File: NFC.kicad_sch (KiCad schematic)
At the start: 3 parts, among them U9 ST25DV04KC

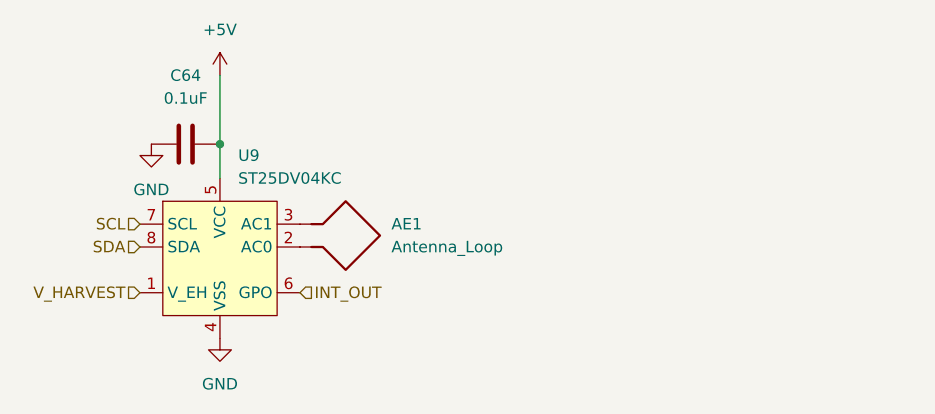
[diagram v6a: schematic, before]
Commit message: added nfc antenna components, added most of footprints
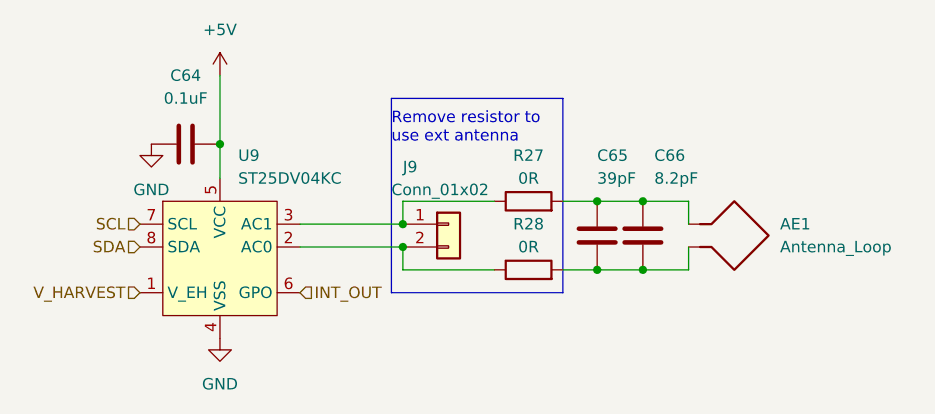
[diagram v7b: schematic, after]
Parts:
- added C65: 39pF, Capacitor_SMD:C_0603_1608Metric_Pad1.08x0.95mm_HandSolder, symbol Device:C
- added C66: 8.2pF, Capacitor_SMD:C_0603_1608Metric_Pad1.08x0.95mm_HandSolder, symbol Device:C
- added J9: Conn_01x02, Connector_PinSocket_2.54mm:PinSocket_1x02_P2.54mm_Vertical, symbol Connector_Generic:Conn_01x02
- added R27, R28: 0R, symbol Device:R
- AE1: footprint (none) -> airsoft_controller:Antenna_loop-13.56MHz
- C64: footprint (none) -> Capacitor_SMD:C_0603_1608Metric_Pad1.08x0.95mm_HandSolder
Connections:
- net at AE1.1: now also C65.1, C66.1, R27.2; no longer U9.3 (AC1)
- net at AE1.2: now also C65.2, C66.2, R28.2; no longer U9.2 (AC0)
- new net: J9.2 (Pin_2), R28.1, U9.2 (AC0)
- new net: J9.1 (Pin_1), R27.1, U9.3 (AC1)
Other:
- note added: "Remove resistor to use ext antenna"
- moved on the sheet: AE1
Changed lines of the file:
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@@
 (kicad_sch (version 20211123) (generator eeschema)
   (paper "A4")
+  (junction (at 187.96 83.82) (diameter 0) (color 0 0 0 0)
+  )
+  (junction (at 187.96 76.2) (diameter 0) (color 0 0 0 0)
+  )
   (junction (at 140.97 69.85) (diameter 0) (color 0 0 0 0)
   )
+  (junction (at 182.88 76.2) (diameter 0) (color 0 0 0 0)
+  )
+  (junction (at 182.88 83.82) (diameter 0) (color 0 0 0 0)
+  )
+  (junction (at 161.29 81.28) (diameter 0) (color 0 0 0 0)
+  )
+  (junction (at 161.29 78.74) (diameter 0) (color 0 0 0 0)
+  )
+  (wire (pts (xy 149.86 81.28) (xy 161.29 81.28))
+    (stroke (width 0) (type default) (color 0 0 0 0))
+  )
+  (wire (pts (xy 171.45 83.82) (xy 161.29 83.82))
+    (stroke (width 0) (type default) (color 0 0 0 0))
+  )
+  (wire (pts (xy 149.86 78.74) (xy 161.29 78.74))
+    (stroke (width 0) (type default) (color 0 0 0 0))
+  )
+  (wire (pts (xy 187.96 76.2) (xy 193.04 76.2))
+    (stroke (width 0) (type default) (color 0 0 0 0))
+  )
+  (polyline (pts (xy 179.07 64.77) (xy 179.07 86.36))
+    (stroke (width 0) (type default) (color 0 0 0 0))
+  )
+  (wire (pts (xy 179.07 76.2) (xy 182.88 76.2))
+    (stroke (width 0) (type default) (color 0 0 0 0))
+  )
+  (wire (pts (xy 161.29 83.82) (xy 161.29 81.28))
+    (stroke (width 0) (type default) (color 0 0 0 0))
+  )
   (wire (pts (xy 140.97 69.85) (xy 140.97 73.66))
     (stroke (width 0) (type default) (color 0 0 0 0))
   )
+  (wire (pts (xy 182.88 83.82) (xy 179.07 83.82))
+    (stroke (width 0) (type default) (color 0 0 0 0))
+  )
+  (wire (pts (xy 193.04 81.28) (xy 193.04 83.82))
+    (stroke (width 0) (type default) (color 0 0 0 0))
+  )
+  (wire (pts (xy 182.88 76.2) (xy 187.96 76.2))
+    (stroke (width 0) (type default) (color 0 0 0 0))
+  )
+  (wire (pts (xy 187.96 83.82) (xy 182.88 83.82))
+    (stroke (width 0) (type default) (color 0 0 0 0))
+  )
+  (polyline (pts (xy 160.02 64.77) (xy 179.07 64.77))
+    (stroke (width 0) (type default) (color 0 0 0 0))
+  )
+  (wire (pts (xy 171.45 76.2) (xy 161.29 76.2))
+    (stroke (width 0) (type default) (color 0 0 0 0))
+  )
+  (wire (pts (xy 193.04 78.74) (xy 193.04 76.2))
+    (stroke (width 0) (type default) (color 0 0 0 0))
+  )
+  (polyline (pts (xy 179.07 86.36) (xy 160.02 86.36))
+    (stroke (width 0) (type default) (color 0 0 0 0))
+  )
+  (polyline (pts (xy 160.02 86.36) (xy 160.02 64.77))
+    (stroke (width 0) (type default) (color 0 0 0 0))
+  )
   (wire (pts (xy 140.97 62.23) (xy 140.97 69.85))
     (stroke (width 0) (type default) (color 0 0 0 0))
+  )
+  (wire (pts (xy 193.04 83.82) (xy 187.96 83.82))
+    (stroke (width 0) (type default) (color 0 0 0 0))
+  )
+  (wire (pts (xy 161.29 76.2) (xy 161.29 78.74))
+    (stroke (width 0) (type default) (color 0 0 0 0))
+  )
+  (text "Remove resistor to\nuse ext antenna" (at 160.02 69.85 0)
+    (effects (font (size 1.27 1.27)) (justify left bottom))
   )
   (hierarchical_label "INT_OUT" (shape input) (at 149.86 86.36 0)
@@
     (pin "1")
   )
-  (symbol (lib_id "Device:Antenna_Loop") (at 154.94 78.74 270) (unit 1)
-    (in_bom yes) (on_board yes) (fields_autoplaced)
-    (property "Reference" "AE1" (id 0) (at 160.02 78.7399 90)
-      (effects (font (size 1.27 1.27)) (justify left))
-    )
-    (property "Value" "Antenna_Loop" (id 1) (at 160.02 81.2799 90)
-      (effects (font (size 1.27 1.27)) (justify left))
-    )
-    (property "Footprint" "" (id 2) (at 154.94 78.74 0)
-      (effects (font (size 1.27 1.27)) hide)
-    )
-    (property "Datasheet" "~" (id 3) (at 154.94 78.74 0)
+  (symbol (lib_id "Device:Antenna_Loop") (at 198.12 78.74 270) (unit 1)
+    (in_bom yes) (on_board yes) (fields_autoplaced)
+    (property "Reference" "AE1" (id 0) (at 203.2 78.7399 90)
+      (effects (font (size 1.27 1.27)) (justify left))
+    )
+    (property "Value" "Antenna_Loop" (id 1) (at 203.2 81.2799 90)
+      (effects (font (size 1.27 1.27)) (justify left))
+    )
+    (property "Footprint" "airsoft_controller:Antenna_loop-13.56MHz" (id 2) (at 198.12 78.74 0)
+      (effects (font (size 1.27 1.27)) hide)
+    )
+    (property "Datasheet" "~" (id 3) (at 198.12 78.74 0)
+      (effects (font (size 1.27 1.27)) hide)
+    )
+    (pin "1")
+    (pin "2")
+  )
+  (symbol (lib_id "Device:C") (at 182.88 80.01 0) (unit 1)
+    (in_bom yes) (on_board yes)
+    (property "Reference" "C65" (id 0) (at 182.88 71.12 0)
+      (effects (font (size 1.27 1.27)) (justify left))
+    )
+    (property "Value" "39pF" (id 1) (at 182.88 73.66 0)
+      (effects (font (size 1.27 1.27)) (justify left))
+    )
+    (property "Footprint" "Capacitor_SMD:C_0603_1608Metric_Pad1.08x0.95mm_HandSolder" (id 2) (at 183.8452 83.82 0)
+      (effects (font (size 1.27 1.27)) hide)
+    )
+    (property "Datasheet" "~" (id 3) (at 182.88 80.01 0)
       (effects (font (size 1.27 1.27)) hide)
     )
@@
     (property "Reference" "C64" (id 0) (at 137.16 62.23 90))
     (property "Value" "0.1uF" (id 1) (at 137.16 64.77 90))
-    (property "Footprint" "" (id 2) (at 140.97 68.8848 0)
+    (property "Footprint" "Capacitor_SMD:C_0603_1608Metric_Pad1.08x0.95mm_HandSolder" (id 2) (at 140.97 68.8848 0)
       (effects (font (size 1.27 1.27)) hide)
     )
@@
       (effects (font (size 1.27 1.27)) hide)
     )
+    (pin "1")
+    (pin "2")
+  )
+  (symbol (lib_id "Connector_Generic:Conn_01x02") (at 166.37 78.74 0) (unit 1)
+    (in_bom yes) (on_board yes)
+    (property "Reference" "J9" (id 0) (at 161.29 72.39 0)
+      (effects (font (size 1.27 1.27)) (justify left))
+    )
+    (property "Value" "Conn_01x02" (id 1) (at 160.02 74.93 0)
+      (effects (font (size 1.27 1.27)) (justify left))
+    )
+    (property "Footprint" "Connector_PinSocket_2.54mm:PinSocket_1x02_P2.54mm_Vertical" (id 2) (at 166.37 78.74 0)
+      (effects (font (size 1.27 1.27)) hide)
+    )
+    (property "Datasheet" "~" (id 3) (at 166.37 78.74 0)
+      (effects (font (size 1.27 1.27)) hide)
+    )
+    (pin "1")
+    (pin "2")
+  )
+  (symbol (lib_id "Device:R") (at 175.26 83.82 90) (unit 1)
+    (in_bom yes) (on_board yes)
+    (property "Reference" "R28" (id 0) (at 175.26 78.74 90))
+    (property "Value" "0R" (id 1) (at 175.26 81.28 90))
+    (property "Footprint" "" (id 2) (at 175.26 85.598 90)
+      (effects (font (size 1.27 1.27)) hide)
+    )
+    (property "Datasheet" "~" (id 3) (at 175.26 83.82 0)
+      (effects (font (size 1.27 1.27)) hide)
+    )
+    (pin "1")
+    (pin "2")
+  )
+  (symbol (lib_id "Device:C") (at 187.96 80.01 0) (unit 1)
+    (in_bom yes) (on_board yes)
+    (property "Reference" "C66" (id 0) (at 189.23 71.12 0)
+      (effects (font (size 1.27 1.27)) (justify left))
+    )
+    (property "Value" "8.2pF" (id 1) (at 189.23 73.66 0)
+      (effects (font (size 1.27 1.27)) (justify left))
+    )
+    (property "Footprint" "Capacitor_SMD:C_0603_1608Metric_Pad1.08x0.95mm_HandSolder" (id 2) (at 188.9252 83.82 0)
+      (effects (font (size 1.27 1.27)) hide)
+    )
+    (property "Datasheet" "~" (id 3) (at 187.96 80.01 0)
+      (effects (font (size 1.27 1.27)) hide)
+    )
+    (pin "1")
+    (pin "2")
+  )
+  (symbol (lib_id "Device:R") (at 175.26 76.2 90) (unit 1)
+    (in_bom yes) (on_board yes)
+    (property "Reference" "R27" (id 0) (at 175.26 71.12 90))
+    (property "Value" "0R" (id 1) (at 175.26 73.66 90))
+    (property "Footprint" "" (id 2) (at 175.26 77.978 90)
+      (effects (font (size 1.27 1.27)) hide)
+    )
+    (property "Datasheet" "~" (id 3) (at 175.26 76.2 0)
+      (effects (font (size 1.27 1.27)) hide)
+    )

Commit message: schematic creation
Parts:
- removed J9: Conn_01x02, Connector_PinSocket_2.54mm:PinSocket_1x02_P2.54mm_Vertical, symbol Connector_Generic:Conn_01x02
- R25: renamed from R27; footprint (none) -> Resistor_SMD:R_0603_1608Metric_Pad0.98x0.95mm_HandSolder
- R26: renamed from R28; footprint (none) -> Resistor_SMD:R_0603_1608Metric_Pad0.98x0.95mm_HandSolder
- renumbered C64 to C66, C65 to C67, C66 to C68
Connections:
- net EXT_AC0: now reaches R26.1, U9.2 (AC0)
- net EXT_AC1: now reaches R25.1, U9.3 (AC1)
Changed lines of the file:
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@@
   (junction (at 182.88 83.82) (diameter 0) (color 0 0 0 0)
-  )
-  (junction (at 161.29 81.28) (diameter 0) (color 0 0 0 0)
-  )
-  (junction (at 161.29 78.74) (diameter 0) (color 0 0 0 0)
   )
   (wire (pts (xy 149.86 81.28) (xy 161.29 81.28))
@@
     (effects (font (size 1.27 1.27)) (justify right))
   )
+  (hierarchical_label "EXT_AC0" (shape input) (at 161.29 81.28 0)
+    (effects (font (size 1.27 1.27)) (justify left))
+  )
   (hierarchical_label "SDA" (shape input) (at 132.08 81.28 180)
     (effects (font (size 1.27 1.27)) (justify right))
   )
+  (hierarchical_label "EXT_AC1" (shape input) (at 161.29 78.74 0)
+    (effects (font (size 1.27 1.27)) (justify left))
+  )
   (hierarchical_label "V_HARVEST" (shape input) (at 132.08 86.36 180)
     (effects (font (size 1.27 1.27)) (justify right))
@@
   (symbol (lib_id "power:GND") (at 133.35 69.85 0) (unit 1)
     (in_bom yes) (on_board yes) (fields_autoplaced)
-    (property "Reference" "#PWR073" (id 0) (at 133.35 76.2 0)
+    (property "Reference" "#PWR078" (id 0) (at 133.35 76.2 0)
       (effects (font (size 1.27 1.27)) hide)
     )
@@
   (symbol (lib_id "power:GND") (at 140.97 91.44 0) (unit 1)
     (in_bom yes) (on_board yes) (fields_autoplaced)
-    (property "Reference" "#PWR075" (id 0) (at 140.97 97.79 0)
+    (property "Reference" "#PWR080" (id 0) (at 140.97 97.79 0)
       (effects (font (size 1.27 1.27)) hide)
     )
@@
   (symbol (lib_id "Device:C") (at 182.88 80.01 0) (unit 1)
     (in_bom yes) (on_board yes)
-    (property "Reference" "C65" (id 0) (at 182.88 71.12 0)
+    (property "Reference" "C67" (id 0) (at 182.88 71.12 0)
       (effects (font (size 1.27 1.27)) (justify left))
     )
@@
   (symbol (lib_id "power:+5V") (at 140.97 62.23 0) (unit 1)
     (in_bom yes) (on_board yes) (fields_autoplaced)
-    (property "Reference" "#PWR074" (id 0) (at 140.97 66.04 0)
+    (property "Reference" "#PWR079" (id 0) (at 140.97 66.04 0)
       (effects (font (size 1.27 1.27)) hide)
     )
@@
   (symbol (lib_id "Device:C") (at 137.16 69.85 90) (unit 1)
     (in_bom yes) (on_board yes) (fields_autoplaced)
-    (property "Reference" "C64" (id 0) (at 137.16 62.23 90))
+    (property "Reference" "C66" (id 0) (at 137.16 62.23 90))
     (property "Value" "0.1uF" (id 1) (at 137.16 64.77 90))
     (property "Footprint" "Capacitor_SMD:C_0603_1608Metric_Pad1.08x0.95mm_HandSolder" (id 2) (at 140.97 68.8848 0)
@@
     (pin "2")
   )
-  (symbol (lib_id "Connector_Generic:Conn_01x02") (at 166.37 78.74 0) (unit 1)
-    (in_bom yes) (on_board yes)
-    (property "Reference" "J9" (id 0) (at 161.29 72.39 0)
-      (effects (font (size 1.27 1.27)) (justify left))
-    )
-    (property "Value" "Conn_01x02" (id 1) (at 160.02 74.93 0)
-      (effects (font (size 1.27 1.27)) (justify left))
-    )
-    (property "Footprint" "Connector_PinSocket_2.54mm:PinSocket_1x02_P2.54mm_Vertical" (id 2) (at 166.37 78.74 0)
-      (effects (font (size 1.27 1.27)) hide)
-    )
-    (property "Datasheet" "~" (id 3) (at 166.37 78.74 0)
-      (effects (font (size 1.27 1.27)) hide)
-    )
-    (pin "1")
-    (pin "2")
-  )
   (symbol (lib_id "Device:R") (at 175.26 83.82 90) (unit 1)
     (in_bom yes) (on_board yes)
-    (property "Reference" "R28" (id 0) (at 175.26 78.74 90))
+    (property "Reference" "R26" (id 0) (at 175.26 78.74 90))
     (property "Value" "0R" (id 1) (at 175.26 81.28 90))
-    (property "Footprint" "" (id 2) (at 175.26 85.598 90)
+    (property "Footprint" "Resistor_SMD:R_0603_1608Metric_Pad0.98x0.95mm_HandSolder" (id 2) (at 175.26 85.598 90)
       (effects (font (size 1.27 1.27)) hide)
     )
@@
   (symbol (lib_id "Device:C") (at 187.96 80.01 0) (unit 1)
     (in_bom yes) (on_board yes)
-    (property "Reference" "C66" (id 0) (at 189.23 71.12 0)
+    (property "Reference" "C68" (id 0) (at 189.23 71.12 0)
       (effects (font (size 1.27 1.27)) (justify left))
     )
@@
   (symbol (lib_id "Device:R") (at 175.26 76.2 90) (unit 1)
     (in_bom yes) (on_board yes)
-    (property "Reference" "R27" (id 0) (at 175.26 71.12 90))
+    (property "Reference" "R25" (id 0) (at 175.26 71.12 90))
     (property "Value" "0R" (id 1) (at 175.26 73.66 90))
-    (property "Footprint" "" (id 2) (at 175.26 77.978 90)
-      (effects (font (size 1.27 1.27)) hide)
-    )
+    (property "Footprint" "Resistor_SMD:R_0603_1608Metric_Pad0.98x0.95mm_HandSolder" (id 2) (at 175.26 77.978 90)
+      (effects (font (size 1.27 1.27)) hide)
+    )
